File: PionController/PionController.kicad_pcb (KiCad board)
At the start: 4 copper layers, 80 parts, among them J1 SM10B-ULHK-1TA1-ETB_HF_, J2 Conn_01x02, J3 Conn_01x02, J4 Conn_01x02, J6 Conn_01x02, J7 FTSH-107-01-L-DV-K-A, U1 STM32H743VITx, U2 TLV75733PDBV, U3 ISO1050DUB, U4 ISO1050DUB, U5 CA-IS3740HN, X1 ASE-16.00MHz, Y2 32.768kHZ

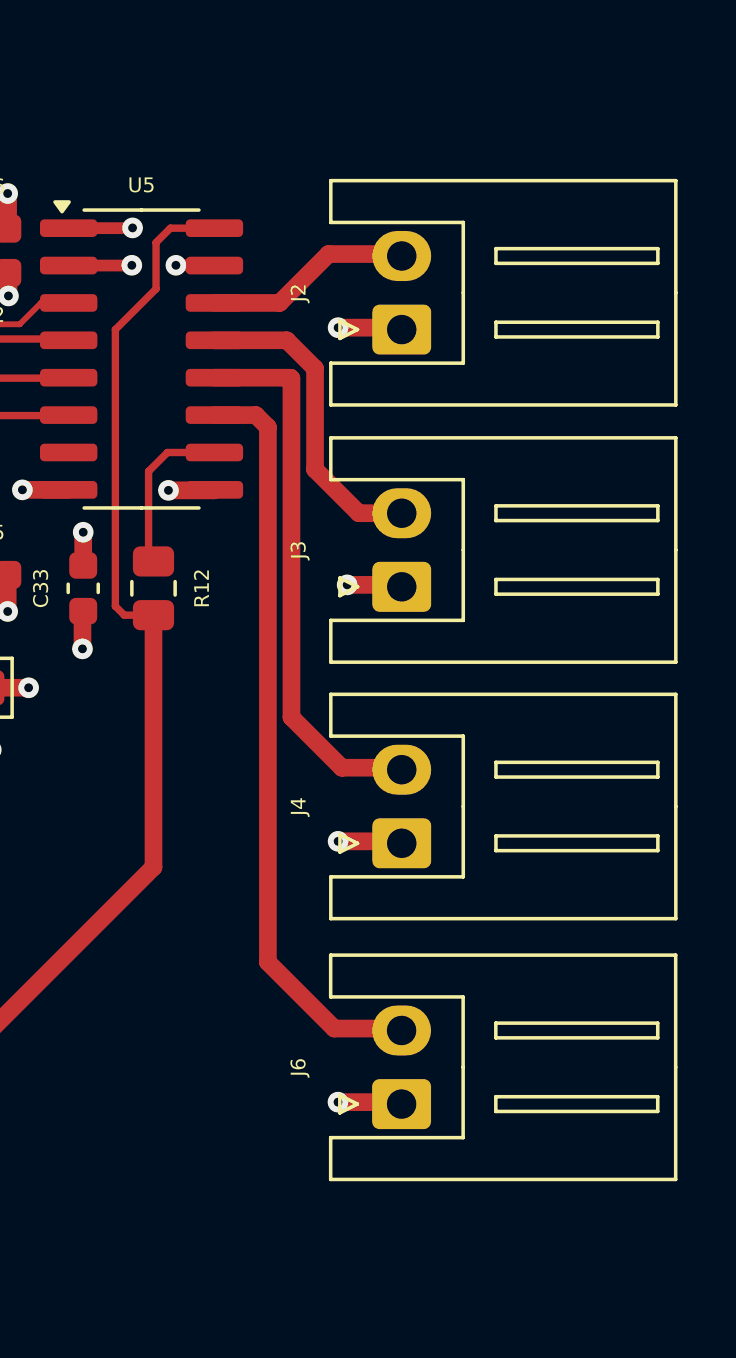
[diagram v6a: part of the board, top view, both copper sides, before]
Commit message: Version 1.3 the gpio lines are thinner making the board a little shorter
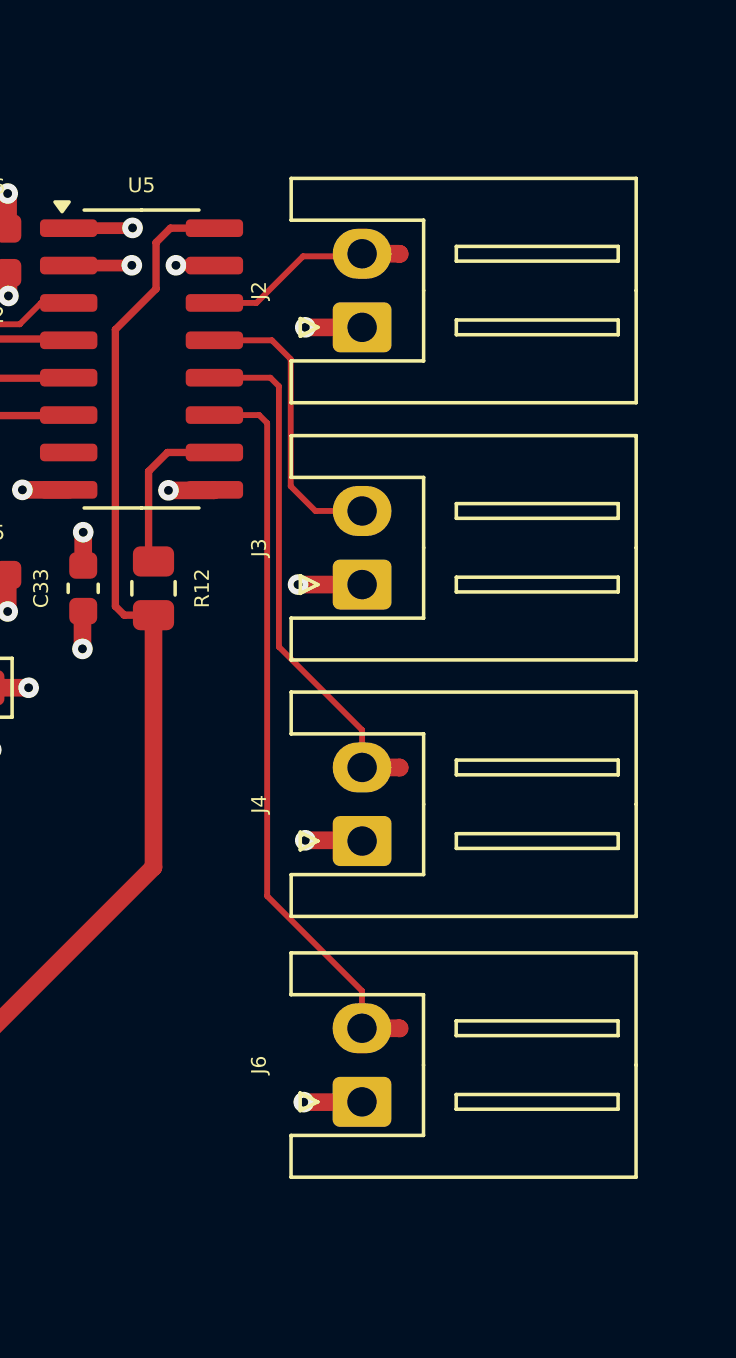
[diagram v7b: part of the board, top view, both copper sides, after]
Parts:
- moved J2 1.35 mm to (172.6, 84.8)
- moved J3 1.35 mm to (172.6, 93.5)
- moved J4 1.35 mm to (172.6, 102.2)
- moved J6 1.35 mm to (172.6, 111.1)
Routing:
- net Net-(J4-Pin_2): track 18.6 -> 17.7 mm
- net Net-(J3-Pin_2): track 10.8 -> 9.95 mm
- net Net-(J6-Pin_2): track 25.7 -> 25.1 mm
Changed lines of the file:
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@@
 	(footprint "Connector_JST:JST_XH_S2B-XH-A_1x02_P2.50mm_Horizontal"
 		(layer "F.Cu")
-		(at 173.9138 102.3112 90)
+		(at 172.5676 102.235 90)
 		(descr "JST XH series connector, S2B-XH-A (http://www.jst-mfg.com/product/pdf/eng/eXH.pdf), generated with kicad-footprint-generator")
 		(tags "connector JST XH horizontal")
@@
 	(footprint "Connector_JST:JST_XH_S2B-XH-A_1x02_P2.50mm_Horizontal"
 		(layer "F.Cu")
-		(at 173.9138 84.8614 90)
+		(at 172.5676 84.7852 90)
 		(descr "JST XH series connector, S2B-XH-A (http://www.jst-mfg.com/product/pdf/eng/eXH.pdf), generated with kicad-footprint-generator")
 		(tags "connector JST XH horizontal")
@@
 	(footprint "Connector_JST:JST_XH_S2B-XH-A_1x02_P2.50mm_Horizontal"
 		(layer "F.Cu")
-		(at 173.9094 111.1704 90)
+		(at 172.5632 111.0942 90)
 		(descr "JST XH series connector, S2B-XH-A (http://www.jst-mfg.com/product/pdf/eng/eXH.pdf), generated with kicad-footprint-generator")
 		(tags "connector JST XH horizontal")
@@
 	(footprint "Connector_JST:JST_XH_S2B-XH-A_1x02_P2.50mm_Horizontal"
 		(layer "F.Cu")
-		(at 173.9138 93.599 90)
+		(at 172.5676 93.5228 90)
 		(descr "JST XH series connector, S2B-XH-A (http://www.jst-mfg.com/product/pdf/eng/eXH.pdf), generated with kicad-footprint-generator")
 		(tags "connector JST XH horizontal")
@@
 	)
 	(segment
-		(start 173.8479 93.5331)
-		(end 173.9138 93.599)
-		(width 0.6)
-		(layer "F.Cu")
-		(net 68)
-	)
-	(segment
 		(start 113.2108 90.7542)
 		(end 113.225 90.74)
@@
 	)
 	(segment
-		(start 171.7522 102.2453)
-		(end 173.8479 102.2453)
-		(width 0.6)
-		(layer "F.Cu")
-		(net 68)
-	)
-	(segment
 		(start 127.9854 113.411)
 		(end 127.9892 113.4148)
@@
 	)
 	(segment
+		(start 170.6372 102.2096)
+		(end 172.5422 102.2096)
+		(width 0.6)
+		(layer "F.Cu")
+		(net 68)
+	)
+	(segment
 		(start 157.1484 93.6752)
 		(end 157.154 93.6808)
@@
 	)
 	(segment
+		(start 170.5864 111.1045)
+		(end 172.5529 111.1045)
+		(width 0.6)
+		(layer "F.Cu")
+		(net 68)
+	)
+	(segment
 		(start 115.7732 107.7976)
 		(end 118.2174 107.7976)
@@
 	)
 	(segment
-		(start 171.7478 111.1045)
-		(end 173.8435 111.1045)
-		(width 0.6)
-		(layer "F.Cu")
-		(net 68)
-	)
-	(segment
-		(start 173.8479 102.2453)
-		(end 173.9138 102.3112)
+		(start 170.3918 93.5228)
+		(end 172.5676 93.5228)
 		(width 0.6)
 		(layer "F.Cu")
@@
 	)
 	(segment
-		(start 173.8479 84.7955)
-		(end 173.9138 84.8614)
+		(start 172.5529 111.1045)
+		(end 172.5632 111.0942)
 		(width 0.6)
 		(layer "F.Cu")
@@
 	)
 	(segment
+		(start 170.6372 84.7852)
+		(end 172.5676 84.7852)
+		(width 0.6)
+		(layer "F.Cu")
+		(net 68)
+	)
+	(segment
 		(start 151.4602 98.7174)
 		(end 153.0096 98.7174)
@@
 	)
 	(segment
+		(start 172.5422 102.2096)
+		(end 172.5676 102.235)
+		(width 0.6)
+		(layer "F.Cu")
+		(net 68)
+	)
+	(segment
 		(start 110.299 93.79)
 		(end 110.3122 93.7768)
@@
 	)
 	(segment
-		(start 171.7522 84.7955)
-		(end 173.8479 84.7955)
-		(width 0.6)
-		(layer "F.Cu")
-		(net 68)
-	)
-	(segment
 		(start 111.921 96.74)
 		(end 111.9124 96.7486)
@@
 	)
 	(segment
-		(start 173.8435 111.1045)
-		(end 173.9094 111.1704)
-		(width 0.6)
-		(layer "F.Cu")
-		(net 68)
-	)
-	(segment
 		(start 155.2956 82.169)
 		(end 157.1422 82.169)
@@
 		(net 68)
 	)
-	(segment
-		(start 172.0596 93.5331)
-		(end 173.8479 93.5331)
-		(width 0.6)
-		(layer "F.Cu")
-		(net 68)
-	)
 	(via
 		(at 143.637 93.1672)
@@
 	)
 	(via
-		(at 171.7478 111.1045)
+		(at 170.5864 111.1045)
 		(size 0.7)
 		(drill 0.3)
@@
 	)
 	(via
-		(at 172.0596 93.5331)
+		(at 170.3918 93.5228)
 		(size 0.7)
 		(drill 0.3)
@@
 	)
 	(via
-		(at 171.7522 102.2453)
+		(at 170.6372 102.2096)
 		(size 0.7)
 		(drill 0.3)
@@
 	)
 	(via
-		(at 171.7522 84.7955)
+		(at 170.6372 84.7852)
 		(size 0.7)
 		(drill 0.3)
@@
 	)
 	(segment
-		(start 167.5496 83.9558)
-		(end 169.7648 83.9558)
+		(start 173.8479 82.2955)
+		(end 173.8376 82.2852)
 		(width 0.6)
 		(layer "F.Cu")
@@
 	)
 	(segment
-		(start 169.7648 83.9558)
-		(end 171.4251 82.2955)
-		(width 0.6)
+		(start 167.5496 83.9558)
+		(end 168.9774 83.9558)
+		(width 0.2)
 		(layer "F.Cu")
 		(net 113)
 	)
 	(segment
-		(start 171.4251 82.2955)
-		(end 173.8479 82.2955)
-		(width 0.6)
+		(start 170.561 82.3722)
+		(end 172.4806 82.3722)
+		(width 0.2)
 		(layer "F.Cu")
 		(net 113)
 	)
 	(segment
-		(start 173.8479 82.2955)
-		(end 173.9138 82.3614)
+		(start 173.8376 82.2852)
+		(end 172.5676 82.2852)
 		(width 0.6)
 		(layer "F.Cu")
@@
 	)
 	(segment
-		(start 170.011 85.2258)
-		(end 170.9672 86.182)
-		(width 0.6)
+		(start 168.9774 83.9558)
+		(end 170.561 82.3722)
+		(width 0.2)
+		(layer "F.Cu")
+		(net 113)
+	)
+	(segment
+		(start 172.4806 82.3722)
+		(end 172.5676 82.2852)
+		(width 0.2)
+		(layer "F.Cu")
+		(net 113)
+	)
+	(segment
+		(start 167.5496 85.2258)
+		(end 169.503 85.2258)
+		(width 0.2)
 		(layer "F.Cu")
 		(net 114)
 	)
 	(segment
-		(start 170.9672 89.611)
-		(end 172.4552 91.099)
-		(width 0.6)
+		(start 169.503 85.2258)
+		(end 170.1418 85.8646)
+		(width 0.2)
 		(layer "F.Cu")
 		(net 114)
 	)
 	(segment
-		(start 167.5496 85.2258)
-		(end 170.011 85.2258)
-		(width 0.6)
+		(start 170.1418 85.8646)
+		(end 170.1418 90.1826)
+		(width 0.2)
 		(layer "F.Cu")
 		(net 114)
 	)
 	(segment
-		(start 170.9672 86.182)
-		(end 170.9672 89.611)
-		(width 0.6)
+		(start 170.1418 90.1826)
+		(end 170.982 91.0228)
+		(width 0.2)
 		(layer "F.Cu")
 		(net 114)
 	)
 	(segment
-		(start 172.4552 91.099)
-		(end 173.9138 91.099)
-		(width 0.6)
+		(start 170.982 91.0228)
+		(end 172.5676 91.0228)
+		(width 0.2)
 		(layer "F.Cu")
 		(net 114)
 	)
 	(segment
-		(start 171.8813 99.7453)
-		(end 173.8479 99.7453)
-		(width 0.6)
+		(start 169.4522 86.4958)
+		(end 169.7418 86.7854)
+		(width 0.2)
 		(layer "F.Cu")
 		(net 115)
 	)
 	(segment
-		(start 167.5496 86.4958)
-		(end 170.138 86.4958)
-		(width 0.6)
+		(start 169.7418 95.6392)
+		(end 172.5676 98.465)
+		(width 0.2)
 		(layer "F.Cu")
 		(net 115)
 	)
 	(segment
-		(start 170.1672 98.0312)
-		(end 171.8813 99.7453)
+		(start 173.8479 99.7453)
+		(end 173.8376 99.735)
 		(width 0.6)
 		(layer "F.Cu")
@@
 	)
 	(segment
-		(start 170.138 86.4958)
-		(end 170.1672 86.525)
-		(width 0.6)
+		(start 167.5496 86.4958)
+		(end 169.4522 86.4958)
+		(width 0.2)
 		(layer "F.Cu")
 		(net 115)
 	)
 	(segment
-		(start 170.1672 86.525)
-		(end 170.1672 98.0312)
+		(start 173.8376 99.735)
+		(end 172.5676 99.735)
 		(width 0.6)
 		(layer "F.Cu")
@@
 	)
 	(segment
-		(start 173.8479 99.7453)
-		(end 173.9138 99.8112)
-		(width 0.6)
+		(start 169.7418 86.7854)
+		(end 169.7418 95.6392)
+		(width 0.2)
 		(layer "F.Cu")
 		(net 115)
 	)
 	(segment
-		(start 169.3672 106.3498)
-		(end 171.6219 108.6045)
-		(width 0.6)
+		(start 172.5676 98.465)
+		(end 172.5676 99.735)
+		(width 0.2)
+		(layer "F.Cu")
+		(net 115)
+	)
+	(segment
+		(start 169.3418 88.0364)
+		(end 169.3418 104.1028)
+		(width 0.2)
 		(layer "F.Cu")
 		(net 116)
 	)
 	(segment
-		(start 169.3672 88.176601)
-		(end 169.3672 106.3498)
+		(start 173.8332 108.5942)
+		(end 172.5632 108.5942)
 		(width 0.6)
 		(layer "F.Cu")
@@
 	(segment
 		(start 173.8435 108.6045)
-		(end 173.9094 108.6704)
+		(end 173.8332 108.5942)
 		(width 0.6)
 		(layer "F.Cu")
@@
 	)
 	(segment
+		(start 169.0712 87.7658)
+		(end 169.3418 88.0364)
+		(width 0.2)
+		(layer "F.Cu")
+		(net 116)
+	)
+	(segment
 		(start 167.5496 87.7658)
-		(end 168.956399 87.7658)
-		(width 0.6)
+		(end 169.0712 87.7658)
+		(width 0.2)
 		(layer "F.Cu")
 		(net 116)
 	)
 	(segment
-		(start 171.6219 108.6045)
-		(end 173.8435 108.6045)
-		(width 0.6)
+		(start 169.3418 104.1028)
+		(end 172.5632 107.3242)
+		(width 0.2)
 		(layer "F.Cu")
 		(net 116)
 	)
 	(segment
-		(start 168.956399 87.7658)
-		(end 169.3672 88.176601)
-		(width 0.6)
+		(start 172.5632 107.3242)
+		(end 172.5632 108.5942)
+		(width 0.2)
 		(layer "F.Cu")
 		(net 116)

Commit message: version 1.3, fixing small error
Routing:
- net Net-(J6-Pin_2): track 25.1 -> 26.6 mm
- net Net-(J4-Pin_2): track 17.7 -> 19.1 mm
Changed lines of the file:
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@@
 	)
 	(segment
-		(start 169.4522 86.4958)
-		(end 169.7418 86.7854)
-		(width 0.2)
-		(layer "F.Cu")
-		(net 115)
-	)
-	(segment
-		(start 169.7418 95.6392)
-		(end 172.5676 98.465)
+		(start 167.5496 86.4958)
+		(end 169.4522 86.4958)
 		(width 0.2)
 		(layer "F.Cu")
@@
 	)
 	(segment
-		(start 167.5496 86.4958)
-		(end 169.4522 86.4958)
+		(start 169.7418 99.3076)
+		(end 170.1692 99.735)
+		(width 0.2)
+		(layer "F.Cu")
+		(net 115)
+	)
+	(segment
+		(start 169.7418 86.7854)
+		(end 169.7418 99.3076)
+		(width 0.2)
+		(layer "F.Cu")
+		(net 115)
+	)
+	(segment
+		(start 170.1692 99.735)
+		(end 172.5676 99.735)
 		(width 0.2)
 		(layer "F.Cu")
@@
 	)
 	(segment
-		(start 169.7418 86.7854)
-		(end 169.7418 95.6392)
-		(width 0.2)
-		(layer "F.Cu")
-		(net 115)
-	)
-	(segment
-		(start 172.5676 98.465)
-		(end 172.5676 99.735)
+		(start 169.4522 86.4958)
+		(end 169.7418 86.7854)
 		(width 0.2)
 		(layer "F.Cu")
@@
 	(segment
 		(start 169.3418 88.0364)
-		(end 169.3418 104.1028)
+		(end 169.3418 107.9246)
+		(width 0.2)
+		(layer "F.Cu")
+		(net 116)
+	)
+	(segment
+		(start 167.5496 87.7658)
+		(end 169.0712 87.7658)
 		(width 0.2)
 		(layer "F.Cu")
@@
 	)
 	(segment
+		(start 170.0114 108.5942)
+		(end 172.5632 108.5942)
+		(width 0.2)
+		(layer "F.Cu")
+		(net 116)
+	)
+	(segment
 		(start 169.0712 87.7658)
 		(end 169.3418 88.0364)
@@
 	)
 	(segment
-		(start 167.5496 87.7658)
-		(end 169.0712 87.7658)
+		(start 169.3418 107.9246)
+		(end 170.0114 108.5942)
 		(width 0.2)
 		(layer "F.Cu")
-		(net 116)
-	)
-	(segment
-		(start 169.3418 104.1028)
-		(end 172.5632 107.3242)
-		(width 0.2)
-		(layer "F.Cu")
-		(net 116)
-	)
-	(segment
-		(start 172.5632 107.3242)
-		(end 172.5632 108.5942)
-		(width 0.2)
-		(layer "F.Cu")
